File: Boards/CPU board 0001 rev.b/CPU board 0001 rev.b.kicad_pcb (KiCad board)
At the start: 2 copper layers, 165.9 x 187.4 mm, 78 parts, among them J1 CEC card edge connector large, U1 SPARE, U10 7432, U11 7442, U12 7406, U13 7406, U14 7442, U15 7442, U16 M8216, U17 M8216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

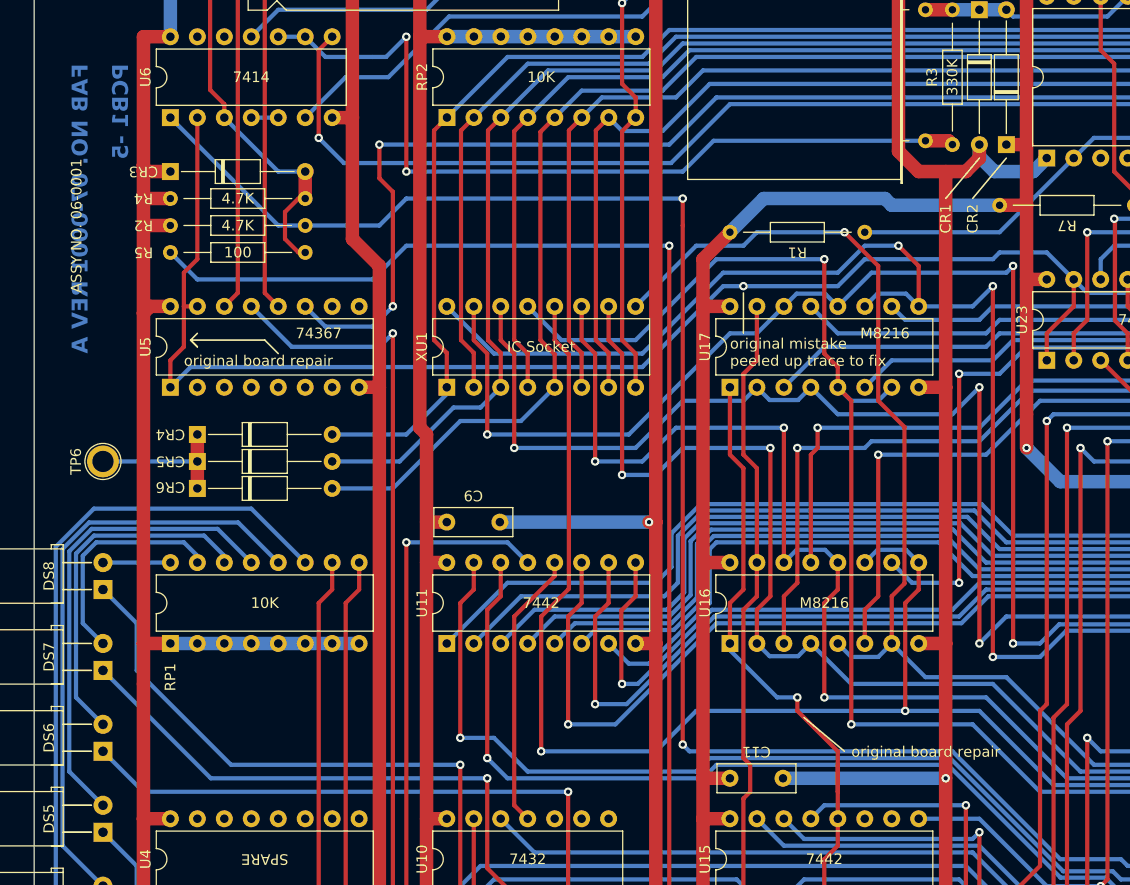
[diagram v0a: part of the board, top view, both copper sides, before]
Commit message: checked Rev.c cpu board and tweaked copper on a and b
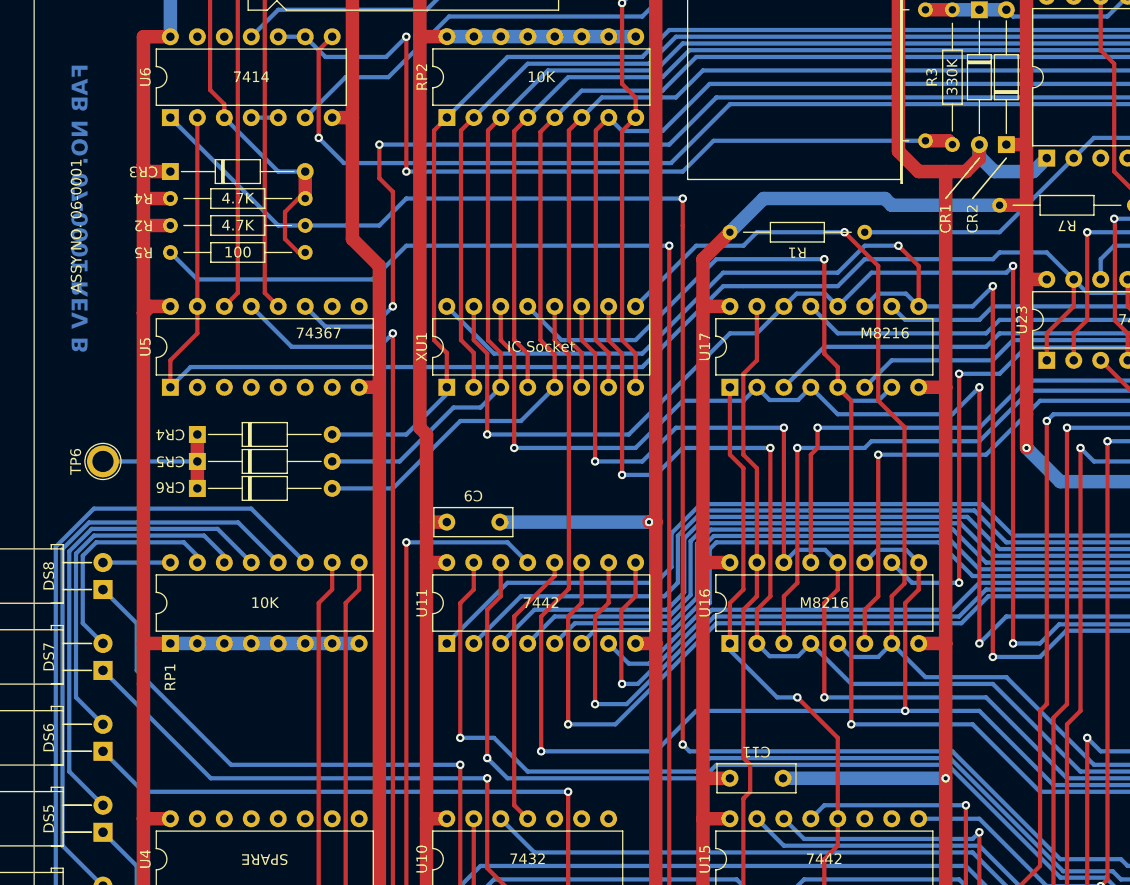
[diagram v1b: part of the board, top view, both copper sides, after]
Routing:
- net Net-(U14-0): track 93.4 -> 90.9 mm
- net Net-(U23-OEa): track 173.1 -> 171.8 mm, vias 3 -> 2
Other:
- board text added: "FAB NO. 07-0001 REV B"
- board text removed: "FAB NO. 07-0001 REV A"
- board text removed: "PCB1 -5"
- board text removed: "original board repair"
- board text removed: "original mistake peeled up trace to fix"
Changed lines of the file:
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@@
   (gr_line (start 130.81 38.1) (end 127.635 41.91)
     (stroke (width 0.15) (type default)) (layer "F.SilkS"))
-  (gr_line (start 57.15 55.88) (end 56.515 55.245)
-    (stroke (width 0.15) (type default)) (layer "F.SilkS"))
-  (gr_line (start 56.515 55.245) (end 57.15 54.61)
-    (stroke (width 0.15) (type default)) (layer "F.SilkS"))
-  (gr_line (start 118.11 93.98) (end 114.3 90.805)
-    (stroke (width 0.15) (type default)) (layer "F.SilkS"))
-  (gr_line (start 56.515 55.245) (end 57.15 55.88)
-    (stroke (width 0.15) (type default)) (layer "F.SilkS"))
-  (gr_line (start 63.5 55.245) (end 56.515 55.245)
-    (stroke (width 0.15) (type default)) (layer "F.SilkS"))
-  (gr_line (start 64.77 56.515) (end 63.5 55.245)
-    (stroke (width 0.15) (type default)) (layer "F.SilkS"))
   (gr_line (start 130.175 41.91) (end 133.35 38.1)
-    (stroke (width 0.15) (type default)) (layer "F.SilkS"))
-  (gr_line (start 108.585 54.61) (end 108.585 50.8)
     (stroke (width 0.15) (type default)) (layer "F.SilkS"))
   (gr_line (start 41.78 187.67) (end 41.78 20.61)
@@
     (effects (font (size 1.5 1.5) (thickness 0.3) bold) (justify left bottom))
   )
-  (gr_text "FAB NO. 07-0001 REV A" (at 46.99 29.21 90) (layer "B.Cu")
+  (gr_text "FAB NO. 07-0001 REV B" (at 46.99 29.21 90) (layer "B.Cu")
     (effects (font (size 1.5 1.5) (thickness 0.3) bold) (justify left bottom mirror))
   )
@@
     (effects (font (size 1.5 1.5) (thickness 0.3) bold) (justify left bottom mirror))
   )
-  (gr_text "PCB1 -5" (at 50.8 29.21 90) (layer "B.Cu")
-    (effects (font (size 1.5 1.5) (thickness 0.3) bold) (justify left bottom mirror))
-  )
   (gr_text "122" (at 207.01 184.15 90) (layer "B.Cu")
     (effects (font (size 1.5 1.5) (thickness 0.3) bold) (justify left bottom mirror))
-  )
-  (gr_text "original board repair" (at 118.745 94.615) (layer "F.SilkS")
-    (effects (font (size 1 1) (thickness 0.15)) (justify left bottom))
   )
   (gr_text "PIZZA TIME\nTHEATER" (at 48.26 175.895 90) (layer "F.SilkS")
     (effects (font (size 1 1) (thickness 0.15)) (justify bottom))
   )
-  (gr_text "original mistake\npeeled up trace to fix" (at 107.315 57.785) (layer "F.SilkS")
-    (effects (font (size 1 1) (thickness 0.15)) (justify left bottom))
-  )
   (gr_text "ASSY NO. 06-0001" (at 46.355 50.8 90) (layer "F.SilkS")
-    (effects (font (size 1 1) (thickness 0.15)) (justify left bottom))
-  )
-  (gr_text "original board repair" (at 55.88 57.785) (layer "F.SilkS")
     (effects (font (size 1 1) (thickness 0.15)) (justify left bottom))
   )
@@
   (segment (start 197.485 180.975) (end 191.135 180.975) (width 0.4) (layer "B.Cu") (net 1))
   (segment (start 187.96 60.96) (end 187.96 23.495) (width 1.27) (layer "F.Cu") (net 2))
+  (segment (start 74.295 185.42) (end 74.295 180.975) (width 1.27) (layer "F.Cu") (net 2))
   (segment (start 185.42 22.86) (end 187.325 24.765) (width 1.27) (layer "F.Cu") (net 2))
   (segment (start 72.39 107.95) (end 74.295 107.95) (width 1.27) (layer "F.Cu") (net 2))
@@
   (segment (start 71.755 34.29) (end 71.755 16.51) (width 1.27) (layer "F.Cu") (net 2))
   (segment (start 207.645 91.44) (end 205.74 93.345) (width 1.27) (layer "F.Cu") (net 2))
-  (segment (start 76.815 187.94) (end 74.295 185.42) (width 1.27) (layer "F.Cu") (net 2))
   (segment (start 125.095 184.15) (end 125.095 180.975) (width 1.27) (layer "F.Cu") (net 2))
   (segment (start 192.405 13.97) (end 190.5 13.97) (width 1.27) (layer "F.Cu") (net 2))
@@
   (segment (start 214.63 60.96) (end 207.645 60.96) (width 1.27) (layer "F.Cu") (net 2))
   (segment (start 137.16 160.02) (end 135.255 160.02) (width 1.27) (layer "F.Cu") (net 2))
-  (segment (start 79.455 187.94) (end 76.815 187.94) (width 1.27) (layer "F.Cu") (net 2))
   (segment (start 117.475 124.46) (end 120.015 121.92) (width 1.27) (layer "F.Cu") (net 2))
   (segment (start 74.295 132.08) (end 74.295 132.715) (width 1.27) (layer "F.Cu") (net 2))
@@
   (segment (start 208.28 114.3) (end 214.63 114.3) (width 1.27) (layer "F.Cu") (net 2))
   (segment (start 93.98 12.7) (end 123.19 12.7) (width 1.27) (layer "F.Cu") (net 2))
-  (segment (start 74.295 185.42) (end 74.295 180.975) (width 1.27) (layer "F.Cu") (net 2))
   (segment (start 123.19 19.05) (end 123.19 12.7) (width 1.27) (layer "F.Cu") (net 2))
   (segment (start 130.81 36.83) (end 130.81 38.1) (width 1.27) (layer "F.Cu") (net 2))
@@
   (segment (start 182.245 65.405) (end 187.325 60.325) (width 1.27) (layer "F.Cu") (net 2))
   (segment (start 125.095 83.82) (end 127.635 83.82) (width 1.27) (layer "F.Cu") (net 2))
+  (segment (start 79.455 187.94) (end 76.815 187.94) (width 1.27) (layer "F.Cu") (net 2))
   (segment (start 122.555 156.835) (end 125.085 156.835) (width 1.27) (layer "F.Cu") (net 2))
   (segment (start 166.37 86.995) (end 167.64 88.265) (width 0.4) (layer "F.Cu") (net 2))
@@
   (segment (start 127.635 39.37) (end 125.095 39.37) (width 1.27) (layer "F.Cu") (net 2))
   (segment (start 101.58 182.225) (end 101.58 173.3) (width 1.27) (layer "F.Cu") (net 2))
+  (segment (start 76.815 187.94) (end 74.295 185.42) (width 1.27) (layer "F.Cu") (net 2))
   (segment (start 205.74 115.57) (end 207.01 115.57) (width 1.27) (layer "F.Cu") (net 2))
   (segment (start 125.095 156.845) (end 125.095 137.16) (width 1.27) (layer "F.Cu") (net 2))
@@
   (segment (start 138.43 15.24) (end 137.795 14.605) (width 0.4) (layer "B.Cu") (net 138))
   (segment (start 116.205 133.985) (end 116.205 104.14) (width 0.4) (layer "F.Cu") (net 139))
+  (segment (start 113.665 88.9) (end 117.475 92.71) (width 0.4) (layer "F.Cu") (net 139))
   (segment (start 107.315 59.69) (end 107.315 66.04) (width 0.4) (layer "F.Cu") (net 139))
-  (segment (start 117.475 93.98) (end 113.665 90.17) (width 0.4) (layer "F.Cu") (net 139))
   (segment (start 108.585 78.74) (end 107.315 80.01) (width 0.4) (layer "F.Cu") (net 139))
   (segment (start 107.315 66.04) (end 108.585 67.31) (width 0.4) (layer "F.Cu") (net 139))
   (segment (start 116.205 104.14) (end 117.475 102.87) (width 0.4) (layer "F.Cu") (net 139))
-  (segment (start 117.475 100.33) (end 117.475 97.79) (width 0.4) (layer "F.Cu") (net 139))
-  (segment (start 117.475 97.79) (end 117.475 95.25) (width 0.4) (layer "F.Cu") (net 139))
-  (segment (start 117.475 97.79) (end 117.475 93.98) (width 0.4) (layer "F.Cu") (net 139))
   (segment (start 108.585 67.31) (end 108.585 78.74) (width 0.4) (layer "F.Cu") (net 139))
+  (segment (start 117.475 92.71) (end 117.475 100.33) (width 0.4) (layer "F.Cu") (net 139))
   (segment (start 117.475 102.87) (end 117.475 100.33) (width 0.4) (layer "F.Cu") (net 139))
-  (segment (start 113.665 90.17) (end 113.665 88.9) (width 0.4) (layer "F.Cu") (net 139))
   (segment (start 107.315 80.01) (end 107.315 83.82) (width 0.4) (layer "F.Cu") (net 139))
   (via (at 113.665 88.9) (size 0.8) (drill 0.4) (layers "F.Cu" "B.Cu") (net 139))
@@
   (segment (start 138.325 82.02) (end 136.525 83.82) (width 0.4) (layer "B.Cu") (net 147))
   (segment (start 139.7 52.07) (end 139.7 49.53) (width 0.4) (layer "F.Cu") (net 148))
-  (segment (start 55.88 55.88) (end 55.88 52.07) (width 0.4) (layer "F.Cu") (net 148))
+  (segment (start 57.15 52.07) (end 57.15 54.61) (width 0.4) (layer "F.Cu") (net 148))
   (segment (start 137.16 54.61) (end 139.7 52.07) (width 0.4) (layer "F.Cu") (net 148))
+  (segment (start 54.61 57.15) (end 54.61 59.69) (width 0.4) (layer "F.Cu") (net 148))
+  (segment (start 57.15 54.61) (end 54.61 57.15) (width 0.4) (layer "F.Cu") (net 148))
   (segment (start 170.18 50.8) (end 170.18 49.53) (width 0.4) (layer "F.Cu") (net 148))
-  (segment (start 54.61 59.69) (end 54.61 57.15) (width 0.4) (layer "F.Cu") (net 148))
   (segment (start 167.64 53.34) (end 170.18 50.8) (width 0.4) (layer "F.Cu") (net 148))
-  (segment (start 55.88 48.895) (end 57.15 47.625) (width 0.4) (layer "F.Cu") (net 148))
-  (segment (start 55.88 52.07) (end 55.88 48.895) (width 0.4) (layer "F.Cu") (net 148))
-  (segment (start 57.15 47.625) (end 57.15 34.29) (width 0.4) (layer "F.Cu") (net 148))
-  (segment (start 54.61 57.15) (end 55.88 55.88) (width 0.4) (layer "F.Cu") (net 148))
+  (segment (start 57.15 34.29) (end 57.15 52.07) (width 0.4) (layer "F.Cu") (net 148))
   (segment (start 137.16 57.15) (end 137.16 54.61) (width 0.4) (layer "F.Cu") (net 148))
-  (segment (start 57.15 52.07) (end 55.88 52.07) (width 0.4) (layer "F.Cu") (net 148))
   (segment (start 167.64 57.15) (end 167.64 53.34) (width 0.4) (layer "F.Cu") (net 148))
   (segment (start 161.925 49.53) (end 161.925 57.15) (width 0.4) (layer "F.Cu") (net 148))
   (via (at 161.925 49.53) (size 0.8) (drill 0.4) (layers "F.Cu" "B.Cu") (net 148))
   (via (at 161.925 57.15) (size 0.8) (drill 0.4) (layers "F.Cu" "B.Cu") (net 148))
-  (via (at 108.585 50.165) (size 0.8) (drill 0.4) (layers "F.Cu" "B.Cu") (net 148))
   (segment (start 132.08 47.625) (end 132.715 46.99) (width 0.4) (layer "B.Cu") (net 148))
   (segment (start 158.75 50.8) (end 160.02 49.53) (width 0.4) (layer "B.Cu") (net 148))

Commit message: updated boards per real one
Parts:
- moved C3 0.63 mm to (58.4, 19.1)
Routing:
- net Net-(U23-OEa): track 171.8 -> 173.7 mm
- net +5V: track 1497.0 -> 1498.9 mm
- net cpu R/~{W}: track 132.6 -> 134.1 mm
- net Net-(CR3-A): track 35.8 -> 34.8 mm

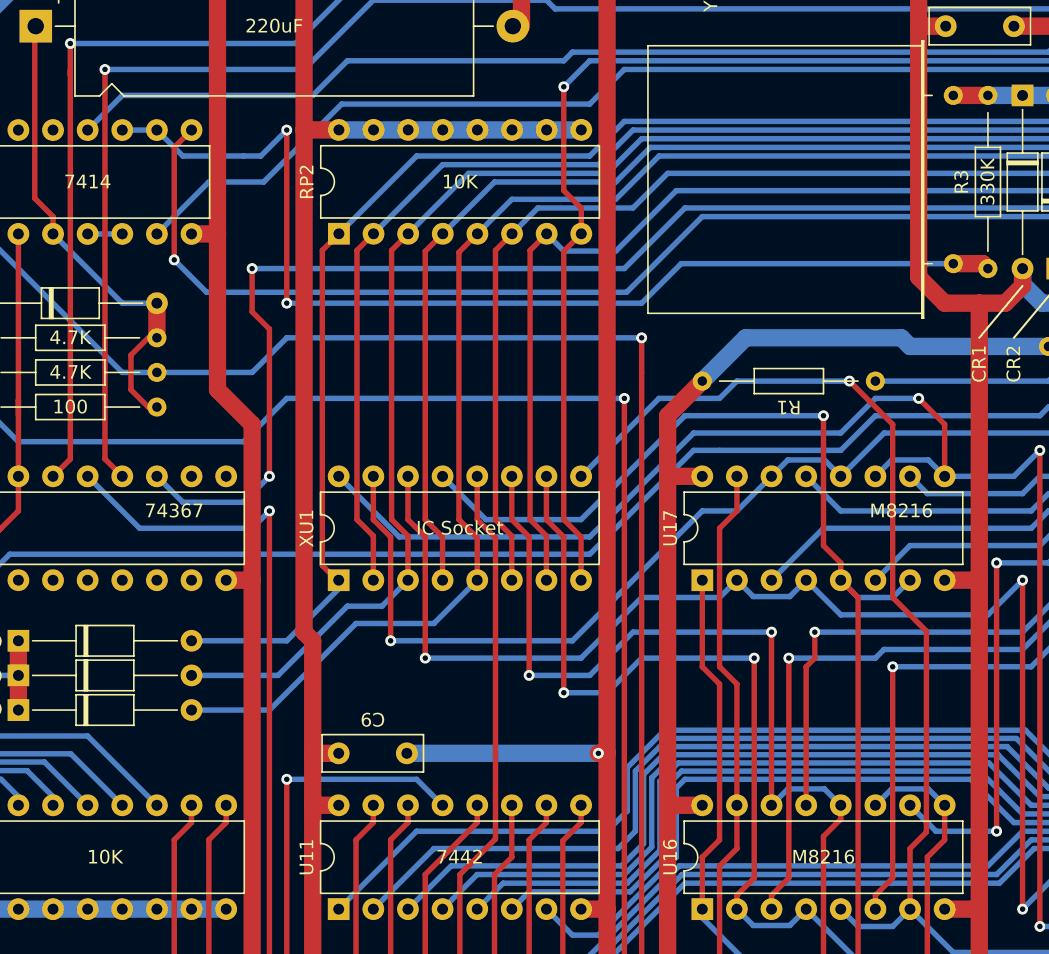
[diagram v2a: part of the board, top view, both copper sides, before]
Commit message: revisions from real life boards
tip130a is actually tip30a, widened holes for crystal, widened holes for big power resistor, fixed cpu board LED resistors
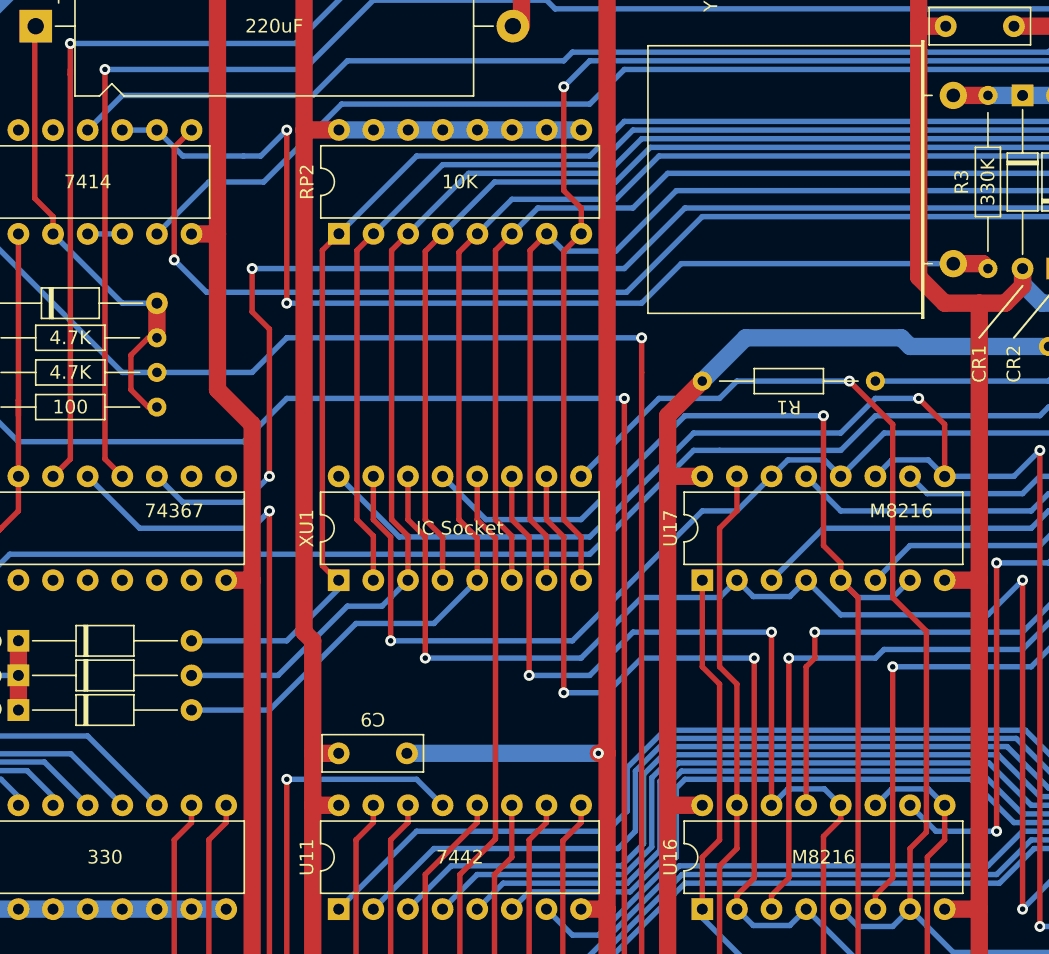
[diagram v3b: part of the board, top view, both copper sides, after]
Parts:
- RP1: value 10K -> 330
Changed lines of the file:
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@@
         (effects (font (size 1 1) (thickness 0.15)))
     )
-    (fp_text value "10K" (at 3.81 8.89 180) (layer "F.SilkS")
+    (fp_text value "330" (at 3.81 8.89 180) (layer "F.SilkS")
         (effects (font (size 1 1) (thickness 0.15)))
     )
@@
     (fp_line (start 16.135 2.5) (end -3.795 2.5)
       (stroke (width 0.1) (type solid)) (layer "F.Fab"))
-    (pad "1" thru_hole circle (at 0 0 270) (size 1.4 1.4) (drill 0.7) (layers "*.Cu" "*.Mask")
+    (pad "1" thru_hole circle (at 0 0 270) (size 2 2) (drill 1) (layers "*.Cu" "*.Mask")
       (net 8 "Net-(CR1-K)") (pinfunction "1") (pintype "passive"))
-    (pad "2" thru_hole circle (at 12.34 0 270) (size 1.4 1.4) (drill 0.7) (layers "*.Cu" "*.Mask")
+    (pad "2" thru_hole circle (at 12.34 0 270) (size 2 2) (drill 1) (layers "*.Cu" "*.Mask")
       (net 114 "Net-(R3-Pad1)") (pinfunction "2") (pintype "passive"))
     (model "${KICAD6_3DMODEL_DIR}/Crystal.3dshapes/Crystal_HC33-U_Horizontal.wrl"
